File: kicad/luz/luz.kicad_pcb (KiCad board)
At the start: 4 copper layers, 49.4 x 21.9 mm, 56 parts, among them J2 Screw_Terminal_01x04, Q1 AO3400A, Q4 AO3400A, U1 U261-241N-4BS2SS, U2 CYPD3177-24LQXQ_C2959321, U4 TPS54302, U5 ESP32-WROOM-32D

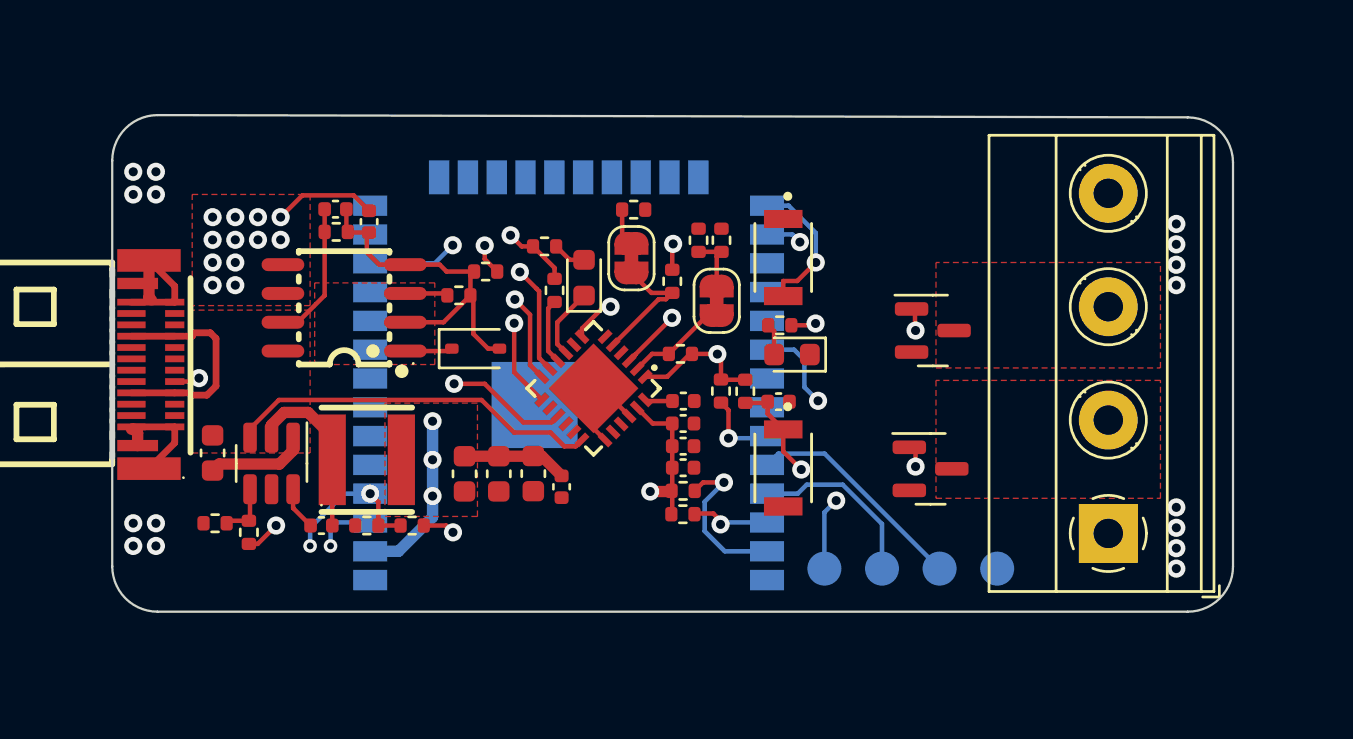
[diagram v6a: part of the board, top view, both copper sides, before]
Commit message: Fix schematic DRC
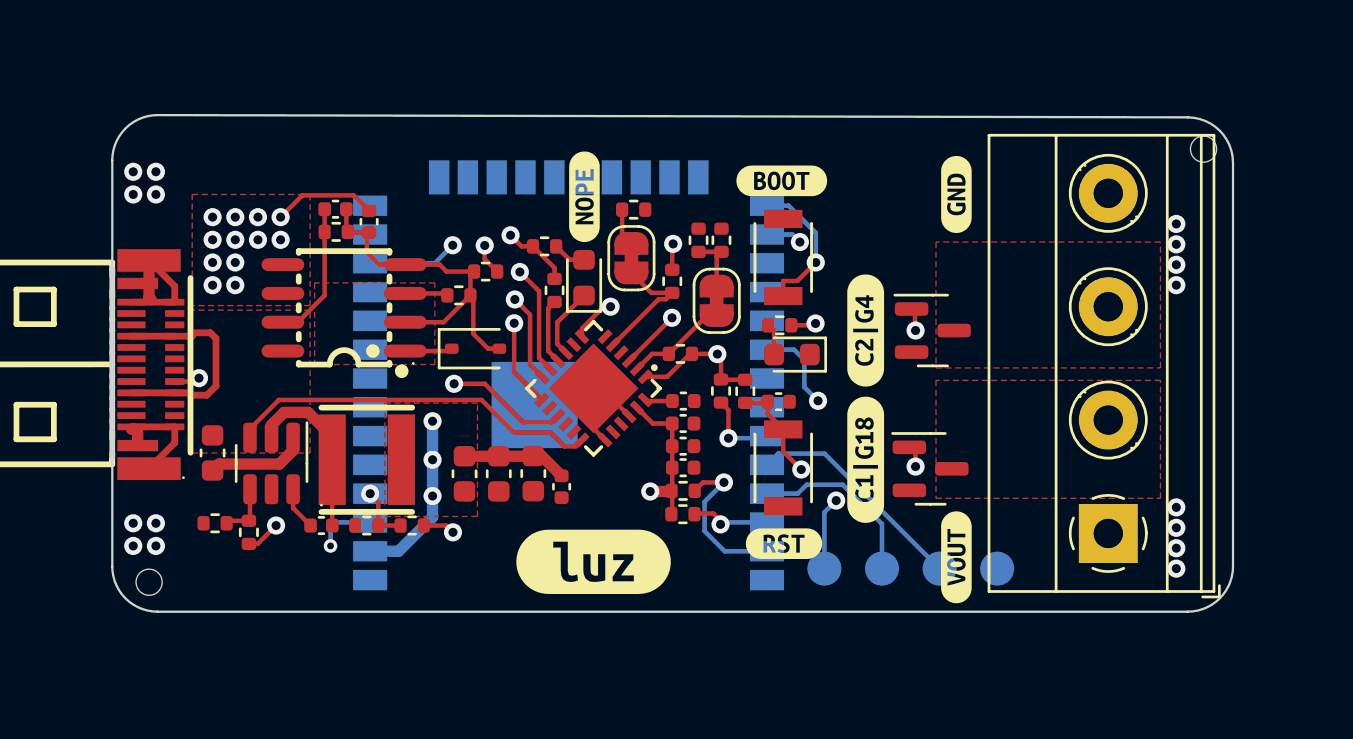
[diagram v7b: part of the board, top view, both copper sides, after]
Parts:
- added ?: , , F.Cu at (80.7, 97.5)
- added REF**: MountingHole_2.1mm, MountingHole:MountingHole_2.1mm, F.Cu at (34.2, 116.6)
- added kibuzzard-655BB3C5: G***, kibuzzard-655BB3C5, F.Cu at (53.4, 99.6)
- added kibuzzard-655BB458: G***, kibuzzard-655BB458, F.Cu at (69.8, 99.5)
- added kibuzzard-655BB485: G***, kibuzzard-655BB485, F.Cu at (69.8, 115.5)
- added kibuzzard-655BB508: G***, kibuzzard-655BB508, B.Cu at (68.6, 97.6)
- added kibuzzard-655BB97E: G***, kibuzzard-655BB97E, F.Cu at (62.1, 98.9)
- added kibuzzard-655BB98B: G***, kibuzzard-655BB98B, F.Cu at (62.2, 114.9)
- added kibuzzard-655BBA1E: G***, kibuzzard-655BBA1E, F.Cu at (65.8, 111.2)
- added kibuzzard-655BBA49: G***, kibuzzard-655BBA49, F.Cu at (65.8, 105.5)
- added kibuzzard-655BBA6D: G***, kibuzzard-655BBA6D, F.Cu at (53.8, 115.7)
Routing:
- net VMon: track 6.61 -> 2.53 mm, vias 2 -> 1

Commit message: Sent 0.0.2a for production
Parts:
- removed kibuzzard-655BB3C5: G***, kibuzzard-655BB3C5
- added kibuzzard-655BC300: G***, kibuzzard-655BC300, F.Cu at (53.4, 99.1)
- L1: value SWPA4030S470MT -> 47uH
- U3: value ~ -> SI4909DY-VB
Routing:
- net GND: vias 16 -> 20
